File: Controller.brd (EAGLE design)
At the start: 100 x 38 mm, 14 parts, among them IC1 74HCT04D, U1 CJT1117-3.3-SOT223

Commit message: added second inverter stage to controller to have non-inverted logic on the outputs
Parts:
- moved IC1 3.00 mm to (22.5, 19.3)
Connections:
- removed net N$54: DATA.2, IC1.2
- removed net N$61: IC1.5, U$12.D0
- new net N$2: IC1.5, IC1.8
- new net N$3: IC1.10, IC1.3
- new net N$4: IC1.1, IC1.12
- new net N$7: IC1.13, U$12.D3
- new net N$8: DATA.4, IC1.2
- net +5V: no longer IC1.11, IC1.13, IC1.9
- net N$60: now also DATA.2; no longer DATA.4
- net N$62: now also IC1.9; no longer IC1.3
- net N$63: now also IC1.11; no longer IC1.1
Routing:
- net N$61: track 42.2 -> 0.00 mm
- net N$63: track 23.3 -> 4.24 mm
- net N$8: track 0.00 -> 18.9 mm
- net N$62: track 20.7 -> 4.24 mm
- net N$54: track 15.0 -> 0.00 mm, vias 2 -> 0
- net +5V: track 49.5 -> 61.9 mm, vias 2 -> 0
- net N$4: track 0.00 -> 7.20 mm
- net N$3: track 0.00 -> 7.20 mm
- net N$2: track 0.00 -> 7.20 mm
- net N$7: track 0.00 -> 4.24 mm
- net N$60: track 14.9 -> 12.9 mm, vias 2 -> 0
- net N$6: track 14.3 -> 15.9 mm
- net GND: track 101.6 -> 103.1 mm

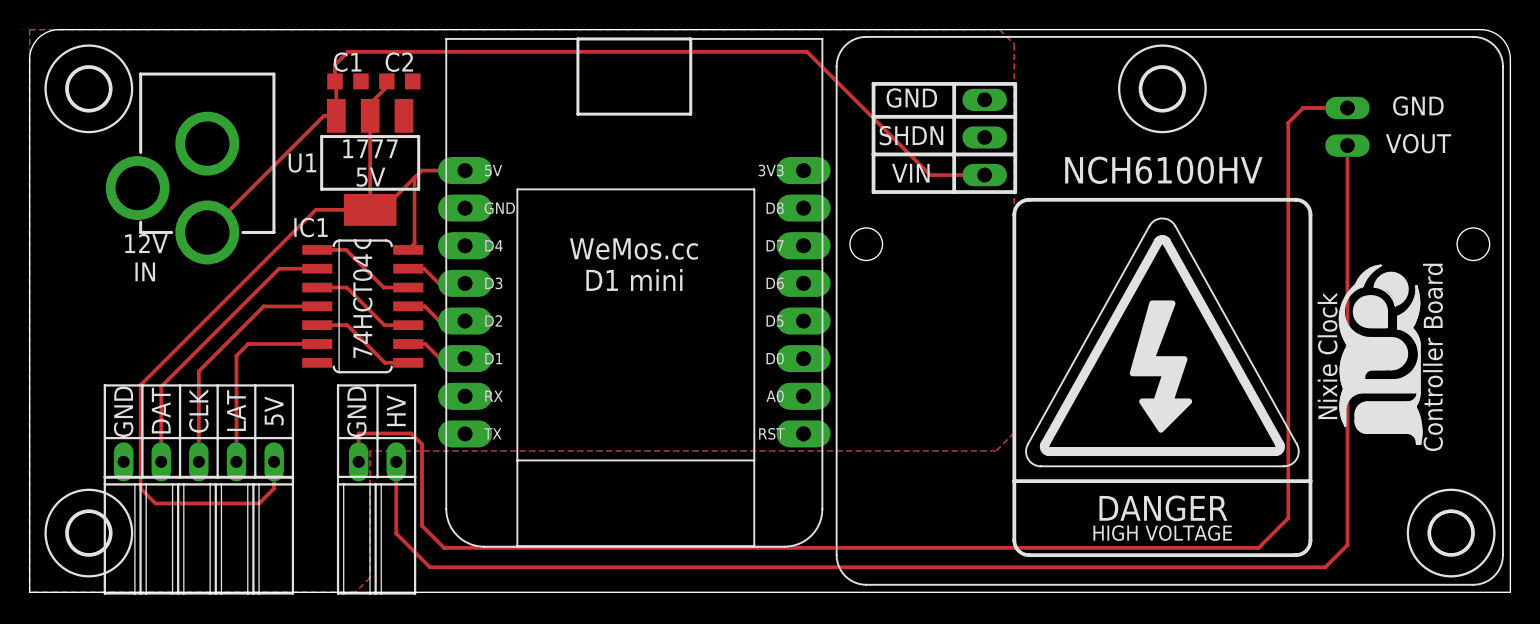
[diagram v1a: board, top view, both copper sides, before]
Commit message: reduced loop area for high-voltage line
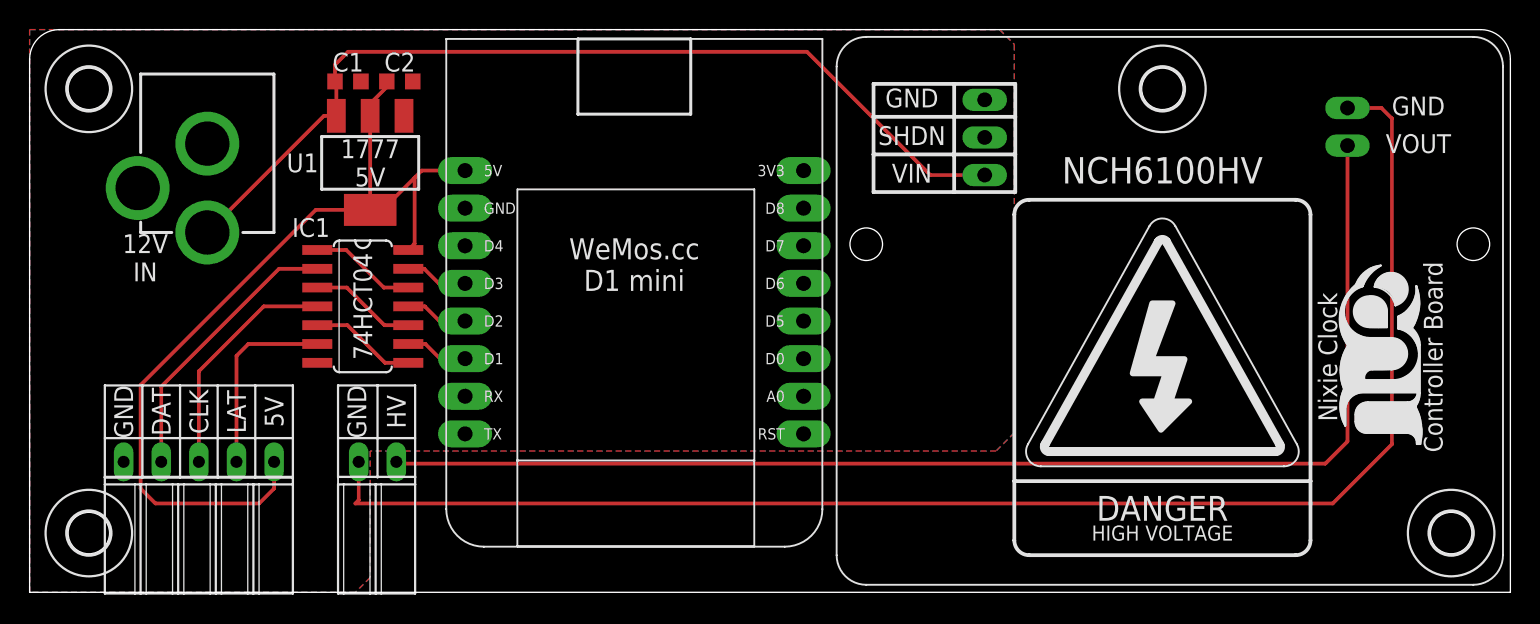
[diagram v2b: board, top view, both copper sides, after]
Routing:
- net N$1: track 97.6 -> 84.9 mm
- net GND: track 103.1 -> 99.9 mm
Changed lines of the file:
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@@
 <drawing>
 <settings>
-<setting alwaysvectorfont="yes"/>
+<setting alwaysvectorfont="no"/>
 <setting verticaltext="up"/>
 </settings>
@@
 <vertex x="22" y="0"/>
 </polygon>
-<wire x1="85" y1="5" x2="83" y2="3" width="0.254" layer="1"/>
-<wire x1="83" y1="3" x2="28" y2="3" width="0.254" layer="1"/>
-<wire x1="28" y1="3" x2="26.5" y2="4.5" width="0.254" layer="1"/>
-<wire x1="85" y1="31.708" x2="85" y2="5" width="0.254" layer="1"/>
-<wire x1="26.5" y1="10" x2="26.5" y2="4.5" width="0.254" layer="1"/>
-<wire x1="22.225" y1="8.81" x2="22.225" y2="10.725" width="0.254" layer="1"/>
-<wire x1="89" y1="32.708" x2="86" y2="32.708" width="0.254" layer="1"/>
-<wire x1="86" y1="32.708" x2="85" y2="31.708" width="0.254" layer="1"/>
-<wire x1="22.225" y1="10.725" x2="25.775" y2="10.725" width="0.254" layer="1"/>
-<wire x1="25.775" y1="10.725" x2="26.5" y2="10" width="0.254" layer="1"/>
 <contactref element="DATA" pad="5"/>
+<wire x1="89" y1="32.708" x2="91.292" y2="32.708" width="0.254" layer="1"/>
+<wire x1="91.292" y1="32.708" x2="92" y2="32" width="0.254" layer="1"/>
+<wire x1="92" y1="32" x2="92" y2="10" width="0.254" layer="1"/>
+<wire x1="92" y1="10" x2="88" y2="6" width="0.254" layer="1"/>
+<wire x1="22" y1="6" x2="88" y2="6" width="0.254" layer="1"/>
+<wire x1="22.225" y1="8.81" x2="22.225" y2="6.225" width="0.254" layer="1"/>
+<wire x1="22.225" y1="6.225" x2="22" y2="6" width="0.254" layer="1"/>
 </signal>
 <signal name="+5V">
@@
 <contactref element="U$1" pad="VOUT"/>
 <contactref element="HV" pad="1"/>
-<wire x1="89" y1="3.19" x2="87.5" y2="1.69" width="0.254" layer="1"/>
-<wire x1="87.5" y1="1.69" x2="27.035" y2="1.69" width="0.254" layer="1"/>
-<wire x1="27.035" y1="1.69" x2="24.765" y2="3.96" width="0.254" layer="1"/>
-<wire x1="24.765" y1="3.96" x2="24.765" y2="8.81" width="0.254" layer="1"/>
-<wire x1="89" y1="30.168" x2="89" y2="3.19" width="0.254" layer="1"/>
+<wire x1="89" y1="10.19" x2="87.5" y2="8.69" width="0.254" layer="1"/>
+<wire x1="87.5" y1="8.69" x2="25.035" y2="8.69" width="0.254" layer="1"/>
+<wire x1="25.035" y1="8.69" x2="24.915" y2="8.81" width="0.254" layer="1"/>
+<wire x1="24.765" y1="8.81" x2="24.915" y2="8.81" width="0.254" layer="1"/>
+<wire x1="89" y1="30.168" x2="89" y2="10.19" width="0.254" layer="1"/>
 </signal>
 <signal name="N$2">

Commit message: moved mounting hole to more accessible location
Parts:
- moved U$4 14.0 mm to (4.00, 18.0)
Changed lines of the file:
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@@
 </layers>
 <board>
-<fusionsync huburn="a.cGVyc29uYWw6dWUyOWFjMzc0" projecturn="a.cGVyc29uYWw6dWUyOWFjMzc0IzIwMTgxMjE1MTY1NzEwMjUx" f3durn="urn:adsk.wipprod:dm.lineage:6qNB6ZptQ1qcPaKZru73zQ" pcbguid="35d47d9c-4b1c-486e-9b1f-d1a53a6c1c47" lastpulledtime="2018-12-16T22:26:32Z" lastsyncedchangeguid="9ef10210-e7d3-09f8-5a0d-b472ea03590e"/>
+<fusionsync huburn="a.cGVyc29uYWw6dWUyOWFjMzc0" projecturn="a.cGVyc29uYWw6dWUyOWFjMzc0IzIwMTgxMjE1MTY1NzEwMjUx" f3durn="urn:adsk.wipprod:dm.lineage:6qNB6ZptQ1qcPaKZru73zQ" pcbguid="35d47d9c-4b1c-486e-9b1f-d1a53a6c1c47" lastpulledtime="2018-12-16T22:26:32Z" lastsyncedchangeguid="de0ec9ff-bd4c-993d-73c5-59805a384694"/>
 <plain>
 <text x="76.5" y="28.5" size="1.778" layer="25" font="fixed" align="center">NCH6100HV</text>
@@
 <element name="U$2" library="OwnStuff" library_urn="urn:adsk.eagle:library:2060095" package="LOGO-SILKSCREEN" package3d_urn="urn:adsk.eagle:package:2060168/1" value="" x="92.25" y="15.89" smashed="yes" rot="R90"/>
 <element name="U$3" library="holes" library_urn="urn:adsk.eagle:library:237" package="2,8" package3d_urn="urn:adsk.eagle:package:14271/1" value="" x="96" y="4" smashed="yes"/>
-<element name="U$4" library="holes" library_urn="urn:adsk.eagle:library:237" package="2,8" package3d_urn="urn:adsk.eagle:package:14271/1" value="" x="4" y="4" smashed="yes"/>
+<element name="U$4" library="holes" library_urn="urn:adsk.eagle:library:237" package="2,8" package3d_urn="urn:adsk.eagle:package:14271/1" value="" x="4" y="18" smashed="yes"/>
 <element name="U$5" library="holes" library_urn="urn:adsk.eagle:library:237" package="2,8" package3d_urn="urn:adsk.eagle:package:14271/1" value="" x="4" y="34" smashed="yes"/>
 <element name="U$6" library="holes" library_urn="urn:adsk.eagle:library:237" package="2,8" package3d_urn="urn:adsk.eagle:package:14271/1" value="" x="76.5" y="34" smashed="yes"/>
